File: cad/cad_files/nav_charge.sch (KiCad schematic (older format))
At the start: 26 parts

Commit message: Bring out battery charge status
LED1 flashes an LED to indicate charging/not-charging/error conditions
Connect it to a hierarchical pin for monitoring by microcontroller
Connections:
- net LED_1a renamed charge_status
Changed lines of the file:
@@
-EESchema Schematic File Version 2  date Tue 02 Dec 2014 10:18:06 PM HST
+EESchema Schematic File Version 2  date Tue 02 Dec 2014 11:16:27 PM HST
 LIBS:local_parts
 LIBS:power
@@
 $Descr A4 11700 8267
 encoding utf-8
-Sheet 2 4
+Sheet 3 4
 Title "Battery Charger"
 Date "3 dec 2014"
@@
 Comment4 ""
 $EndDescr
-Wire Wire Line
-	4200 4200 4200 4100
+Text HLabel 7900 2200 2    60   Output ~ 0
+charge_status
+Wire Wire Line
+	7900 2200 5200 2200
+Wire Wire Line
+	5200 2200 5200 3600
+Connection ~ 5600 3600
+Wire Wire Line
+	5200 3600 5600 3600
+Connection ~ 3800 4100
+Connection ~ 1500 3100
+Wire Wire Line
+	1500 4100 1500 1500
+Wire Wire Line
+	1500 4100 4200 4100
+Wire Wire Line
+	2400 2000 900  2000
+Connection ~ 3800 4900
+Wire Wire Line
+	5200 4900 3800 4900
+Connection ~ 4200 5900
+Wire Wire Line
+	4200 5900 3800 5900
+Wire Wire Line
+	3800 5900 3800 5800
+Wire Wire Line
+	3800 4100 3800 4200
+Wire Wire Line
+	3800 4700 3800 5300
+Wire Wire Line
+	1100 2400 1100 2200
+Wire Wire Line
+	1100 2200 900  2200
+Wire Wire Line
+	1500 3100 1900 3100
+Connection ~ 4000 2000
+Wire Wire Line
+	3900 2000 7700 2000
+Connection ~ 7700 5200
+Wire Wire Line
+	7700 5200 7900 5200
+Wire Wire Line
+	5200 4500 4500 4500
+Connection ~ 6700 6500
+Wire Wire Line
+	6700 6500 6700 5100
+Connection ~ 6000 6500
+Wire Wire Line
+	7700 6500 5800 6500
+Wire Wire Line
+	5800 6500 5800 6400
+Wire Wire Line
+	5800 5700 5800 5900
+Wire Wire Line
+	7600 5300 7700 5300
+Wire Wire Line
+	7100 5300 6800 5300
+Wire Wire Line
+	6800 5300 6800 4900
+Wire Wire Line
+	6800 4900 6600 4900
+Wire Wire Line
+	7700 4200 7700 4500
+Connection ~ 7700 2700
+Wire Wire Line
+	7700 2000 7700 2900
+Wire Wire Line
+	5200 4700 5100 4700
+Wire Wire Line
+	5100 4700 5100 4800
+Wire Wire Line
+	6600 4500 6700 4500
+Wire Wire Line
+	6700 4500 6700 3400
+Connection ~ 7700 3400
+Wire Wire Line
+	6700 3400 7700 3400
+Wire Wire Line
+	5600 2900 5600 3100
+Wire Wire Line
+	5900 3500 5900 3900
+Wire Wire Line
+	5900 2400 5900 1500
+Wire Wire Line
+	6200 3900 6200 3100
+Wire Wire Line
+	6200 3100 6400 3100
+Connection ~ 7000 3100
+Wire Wire Line
+	7000 3100 7000 2700
+Wire Wire Line
+	7000 2700 7100 2700
+Connection ~ 2600 3100
+Wire Wire Line
+	2600 2300 2600 3100
+Wire Wire Line
+	3000 2600 3000 2800
+Wire Wire Line
+	1700 2600 1700 2800
+Wire Wire Line
+	2800 1800 4000 1800
+Wire Wire Line
+	3300 2000 2800 2000
+Connection ~ 2100 2000
+Wire Wire Line
+	1700 2000 1700 2200
+Wire Wire Line
+	2100 2000 2100 2200
+Wire Wire Line
+	2400 1800 2200 1800
+Wire Wire Line
+	2200 1800 2200 2000
+Connection ~ 2200 2000
+Wire Wire Line
+	3000 2200 3000 2000
+Connection ~ 3000 2000
+Wire Wire Line
+	2100 2600 2100 2800
+Wire Wire Line
+	2400 3100 2800 3100
+Connection ~ 1700 2000
+Wire Wire Line
+	3300 3100 4500 3100
+Wire Wire Line
+	6900 3100 7400 3100
+Wire Wire Line
+	7600 2700 7700 2700
+Wire Wire Line
+	5900 2900 5900 3100
+Wire Wire Line
+	5700 3900 5700 3800
+Wire Wire Line
+	5700 3800 5600 3800
+Wire Wire Line
+	5600 3800 5600 3500
+Wire Wire Line
+	5600 2400 5600 2300
+Wire Wire Line
+	5600 2300 5900 2300
+Connection ~ 5900 2300
+Wire Wire Line
+	7700 3600 7700 3300
+Wire Wire Line
+	7700 4300 6900 4300
+Connection ~ 7700 4300
+Wire Wire Line
+	6900 4300 6900 4700
+Wire Wire Line
+	6900 4700 6600 4700
+Wire Wire Line
+	6700 5100 6600 5100
+Wire Wire Line
+	7700 5900 7700 5100
+Connection ~ 7700 5300
+Wire Wire Line
+	6000 5700 6000 5900
+Wire Wire Line
+	6000 6400 6000 6500
+Wire Wire Line
+	6100 6500 6100 5700
+Connection ~ 6100 6500
+Wire Wire Line
+	7700 3500 7900 3500
+Connection ~ 7700 3500
+Wire Wire Line
+	4500 3100 4500 4500
+Wire Wire Line
+	4000 1800 4000 2000
+Connection ~ 1500 2000
+Wire Wire Line
+	4200 4700 4200 5300
+Wire Wire Line
+	4200 5800 4200 6000
+Wire Wire Line
+	7700 6600 7700 6400
+Connection ~ 7700 6500
+Wire Wire Line
+	5200 5100 4200 5100
+Connection ~ 4200 5100
 Wire Wire Line
 	5900 1500 1500 1500
-Connection ~ 4200 5100
-Wire Wire Line
-	5200 5100 4200 5100
-Connection ~ 7700 6500
-Wire Wire Line
-	7700 6400 7700 6600
-Wire Wire Line
-	4200 6000 4200 5800
-Wire Wire Line
-	4200 5300 4200 4700
-Connection ~ 1500 2000
-Wire Wire Line
-	4000 2000 4000 1800
-Wire Wire Line
-	4500 3100 4500 4500
-Connection ~ 7700 3500
-Wire Wire Line
-	7700 3500 7900 3500
-Connection ~ 6100 6500
-Wire Wire Line
-	6100 6500 6100 5700
-Wire Wire Line
-	6000 6400 6000 6500
-Wire Wire Line
-	6000 5700 6000 5900
-Connection ~ 7700 5300
-Wire Wire Line
-	7700 5100 7700 5900
-Wire Wire Line
-	6600 5100 6700 5100
-Wire Wire Line
-	6600 4700 6900 4700
-Wire Wire Line
-	6900 4700 6900 4300
-Connection ~ 7700 4300
-Wire Wire Line
-	6900 4300 7700 4300
-Wire Wire Line
-	7700 3300 7700 3600
-Connection ~ 5900 2300
-Wire Wire Line
-	5900 2300 5600 2300
-Wire Wire Line
-	5600 2300 5600 2400
-Wire Wire Line
-	5600 3500 5600 3600
-Wire Wire Line
-	5600 3600 5700 3600
-Wire Wire Line
-	5700 3600 5700 3900
-Wire Wire Line
-	5900 2900 5900 3100
-Wire Wire Line
-	7600 2700 7700 2700
-Wire Wire Line
-	7400 3100 6900 3100
-Wire Wire Line
-	4500 3100 3300 3100
-Connection ~ 1700 2000
-Wire Wire Line
-	2800 3100 2400 3100
-Wire Wire Line
-	2100 2600 2100 2800
-Connection ~ 3000 2000
-Wire Wire Line
-	3000 2200 3000 2000
-Connection ~ 2200 2000
-Wire Wire Line
-	2200 2000 2200 1800
-Wire Wire Line
-	2200 1800 2400 1800
-Wire Wire Line
-	2100 2000 2100 2200
-Wire Wire Line
-	1700 2000 1700 2200
-Connection ~ 2100 2000
-Wire Wire Line
-	2800 2000 3300 2000
-Wire Wire Line
-	4000 1800 2800 1800
-Wire Wire Line
-	1700 2600 1700 2800
-Wire Wire Line
-	3000 2600 3000 2800
-Wire Wire Line
-	2600 2300 2600 3100
-Connection ~ 2600 3100
-Wire Wire Line
-	7100 2700 7000 2700
-Wire Wire Line
-	7000 2700 7000 3100
-Connection ~ 7000 3100
-Wire Wire Line
-	6400 3100 6200 3100
-Wire Wire Line
-	6200 3100 6200 3900
-Wire Wire Line
-	5900 1500 5900 2400
-Wire Wire Line
-	5900 3500 5900 3900
-Wire Wire Line
-	5600 2900 5600 3100
-Wire Wire Line
-	7700 3400 6700 3400
-Connection ~ 7700 3400
-Wire Wire Line
-	6700 3400 6700 4500
-Wire Wire Line
-	6700 4500 6600 4500
-Wire Wire Line
-	5100 4800 5100 4700
-Wire Wire Line
-	5100 4700 5200 4700
-Wire Wire Line
-	7700 2900 7700 2000
-Connection ~ 7700 2700
-Wire Wire Line
-	7700 4500 7700 4200
-Wire Wire Line
-	6600 4900 6800 4900
-Wire Wire Line
-	6800 4900 6800 5300
-Wire Wire Line
-	6800 5300 7100 5300
-Wire Wire Line
-	7600 5300 7700 5300
-Wire Wire Line
-	5800 5700 5800 5900
-Wire Wire Line
-	5800 6400 5800 6500
-Wire Wire Line
-	5800 6500 7700 6500
-Connection ~ 6000 6500
-Wire Wire Line
-	6700 5100 6700 6500
-Connection ~ 6700 6500
-Wire Wire Line
-	4500 4500 5200 4500
-Wire Wire Line
-	7700 5200 7900 5200
-Connection ~ 7700 5200
-Wire Wire Line
-	7700 2000 3900 2000
-Connection ~ 4000 2000
-Wire Wire Line
-	1500 3100 1900 3100
-Wire Wire Line
-	900  2200 1100 2200
-Wire Wire Line
-	1100 2200 1100 2400
-Wire Wire Line
-	3800 5300 3800 4700
-Wire Wire Line
-	3800 4100 3800 4200
-Wire Wire Line
-	3800 5800 3800 5900
-Wire Wire Line
-	3800 5900 4200 5900
-Connection ~ 4200 5900
-Wire Wire Line
-	5200 4900 3800 4900
-Connection ~ 3800 4900
-Wire Wire Line
-	900  2000 2400 2000
-Wire Wire Line
-	4200 4100 1500 4100
-Wire Wire Line
-	1500 4100 1500 1500
-Connection ~ 1500 3100
-Connection ~ 3800 4100
+Wire Wire Line
+	4200 4100 4200 4200
 Text Notes 8000 3700 0    60   ~ 0
 TODO: power path for charger voltage rail \n  (rather than cutting load power \n    while charging)
@@
 Text Label 5600 3000 2    60   ~ 0
 LED_1b
-Text Label 5700 3800 1    60   ~ 0
+Text Label 5600 3800 2    60   ~ 0
 LED_1a
 Text Label 6700 4900 0    60   ~ 0
@@
 	0    1    -1   0
 $EndComp
-Text Notes 5000 3800 0    60   ~ 0
+Text Notes 5400 4000 2    60   ~ 0
 LED2 prog:\nopen for 2S\nlow for 1S\nhigh for 2P
 Text Notes 8050 6050 0    60   ~ 0

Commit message: Adding refdes details for nav_charge
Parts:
- gave numbers to parts that had none: 17
- renumbered BT1 to BTp101, BT2 to BTp102, R10 to Rp109, R14 to Rp112
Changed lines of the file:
@@
-EESchema Schematic File Version 2  date Wed 03 Dec 2014 11:28:33 AM HST
+EESchema Schematic File Version 2  date Wed 03 Dec 2014 01:00:34 PM HST
 LIBS:local_parts
 LIBS:power
@@
 $EndComp
 $Comp
-L R Rp?
+L R Rp110
 U 1 1 53DA394C
 P 5800 6150
-F 0 "Rp?" V 5880 6150 50  0000 C CNN
+F 0 "Rp110" V 5880 6150 50  0000 C CNN
 F 1 "33k" V 5800 6150 50  0000 C CNN
 	1    5800 6150
@@
 $EndComp
 $Comp
-L R Rp?
+L R Rp111
 U 1 1 53DA3944
 P 6000 6150
-F 0 "Rp?" V 6080 6150 50  0000 C CNN
+F 0 "Rp111" V 6080 6150 50  0000 C CNN
 F 1 "120k" V 6000 6150 50  0000 C CNN
 	1    6000 6150
@@
 $EndComp
 $Comp
-L R R10
+L R Rp109
 U 1 1 53DA275B
 P 7350 5300
-F 0 "R10" V 7430 5300 50  0000 C CNN
+F 0 "Rp109" V 7430 5300 50  0000 C CNN
 F 1 "10" V 7350 5300 50  0000 C CNN
 	1    7350 5300
@@
 $EndComp
 $Comp
-L R R14
+L R Rp112
 U 1 1 53DA26C1
 P 7700 6150
-F 0 "R14" V 7780 6150 50  0000 C CNN
+F 0 "Rp112" V 7780 6150 50  0000 C CNN
 F 1 ".27" V 7700 6150 50  0000 C CNN
 	1    7700 6150
@@
 $EndComp
 $Comp
-L BATTERY BT2
+L BATTERY BTp102
 U 1 1 53DA259B
 P 7700 4800
-F 0 "BT2" H 7700 5000 50  0000 C CNN
+F 0 "BTp102" H 7700 5000 50  0000 C CNN
 F 1 "BATTERY" H 7700 4610 50  0000 C CNN
 	1    7700 4800
@@
 $EndComp
 $Comp
-L BATTERY BT1
+L BATTERY BTp101
 U 1 1 53DA2480
 P 7700 3900
-F 0 "BT1" H 7700 4100 50  0000 C CNN
+F 0 "BTp101" H 7700 4100 50  0000 C CNN
 F 1 "BATTERY" H 7700 3710 50  0000 C CNN
 	1    7700 3900
@@
 $EndComp
 $Comp
-L C C?
+L C Cp103
 U 1 1 53DA230B
 P 5900 3300
-F 0 "C?" H 5950 3400 50  0000 L CNN
+F 0 "Cp103" H 5950 3400 50  0000 L CNN
 F 1 "1uF" H 5950 3200 50  0000 L CNN
 	1    5900 3300
@@
 $EndComp
 $Comp
-L R Rp?
+L R Rp104
 U 1 1 53DA22FE
 P 5900 2650
-F 0 "Rp?" V 5980 2650 50  0000 C CNN
+F 0 "Rp104" V 5980 2650 50  0000 C CNN
 F 1 "150" V 5900 2650 50  0000 C CNN
 	1    5900 2650
@@
 NoConn ~ 5800 3900
 $Comp
-L PNP Qp?
+L PNP Qp102
 U 1 1 53DA21A7
 P 7600 3100
-F 0 "Qp?" H 7600 2950 60  0000 R CNN
+F 0 "Qp102" H 7600 2950 60  0000 R CNN
 F 1 "FCX718" H 7600 3250 60  0000 R CNN
 	1    7600 3100
@@
 $EndComp
 $Comp
-L R Rp?
+L R Rp105
 U 1 1 53DA21A3
 P 7350 2700
-F 0 "Rp?" V 7430 2700 50  0000 C CNN
+F 0 "Rp105" V 7430 2700 50  0000 C CNN
 F 1 "10k" V 7350 2700 50  0000 C CNN
 	1    7350 2700
@@
 $EndComp
 $Comp
-L R Rp?
+L R Rp106
 U 1 1 53DA219B
 P 6650 3100
-F 0 "Rp?" V 6730 3100 50  0000 C CNN
+F 0 "Rp106" V 6730 3100 50  0000 C CNN
 F 1 "100" V 6650 3100 50  0000 C CNN
 	1    6650 3100
@@
 $EndComp
 $Comp
-L R Rp?
+L R Rp103
 U 1 1 53DA2133
 P 5600 2650
-F 0 "Rp?" V 5680 2650 50  0000 C CNN
+F 0 "Rp103" V 5680 2650 50  0000 C CNN
 F 1 "270" V 5600 2650 50  0000 C CNN
 	1    5600 2650
@@
 $EndComp
 $Comp
-L LED D?
+L LED Dp103
 U 1 1 53DA211C
 P 5600 3300
-F 0 "D?" H 5600 3400 50  0000 C CNN
+F 0 "Dp103" H 5600 3400 50  0000 C CNN
 F 1 "LED" H 5600 3200 50  0000 C CNN
 	1    5600 3300
@@
 $EndComp
 $Comp
-L DS2712 Up?
+L DS2712 Up101
 U 1 1 53DA0E27
 P 5900 4800
-F 0 "Up?" H 5900 4700 50  0000 C CNN
+F 0 "Up101" H 5900 4700 50  0000 C CNN
 F 1 "DS2712" H 5900 4900 50  0000 C CNN
 F 2 "MODULE" H 5900 4800 50  0001 C CNN
@@
 $EndComp
 $Comp
-L R Rp?
+L R Rp102
 U 1 1 53DA0CD8
 P 3050 3100
-F 0 "Rp?" V 3130 3100 50  0000 C CNN
+F 0 "Rp102" V 3130 3100 50  0000 C CNN
 F 1 "0" V 3050 3100 50  0000 C CNN
 	1    3050 3100
@@
 $EndComp
 $Comp
-L R Rp?
+L R Rp101
 U 1 1 53DA0CB2
 P 2150 3100
-F 0 "Rp?" V 2230 3100 50  0000 C CNN
+F 0 "Rp101" V 2230 3100 50  0000 C CNN
 F 1 "330" V 2150 3100 50  0000 C CNN
 	1    2150 3100
@@
 $EndComp
 $Comp
-L DIODE D?
+L DIODE Dp102
 U 1 1 53D8CC6B
 P 3000 2400
-F 0 "D?" H 3000 2500 40  0000 C CNN
+F 0 "Dp102" H 3000 2500 40  0000 C CNN
 F 1 "DIODE" H 3000 2300 40  0000 C CNN
 	1    3000 2400
@@
 $EndComp
 $Comp
-L DIODE D?
+L DIODE Dp101
 U 1 1 53D8CC68
 P 2600 1800
-F 0 "D?" H 2600 1900 40  0000 C CNN
+F 0 "Dp101" H 2600 1900 40  0000 C CNN
 F 1 "DIODE" H 2600 1700 40  0000 C CNN
 	1    2600 1800
@@
 $EndComp
 $Comp
-L C C?
+L C Cp102
 U 1 1 53D8CC32
 P 2100 2400
-F 0 "C?" H 2150 2500 50  0000 L CNN
+F 0 "Cp102" H 2150 2500 50  0000 L CNN
 F 1 "0.1uF" H 2150 2300 50  0000 L CNN
 	1    2100 2400
@@
 $EndComp
 $Comp
-L C C?
+L C Cp101
 U 1 1 53D8CC30
 P 1700 2400
-F 0 "C?" H 1750 2500 50  0000 L CNN
+F 0 "Cp101" H 1750 2500 50  0000 L CNN
 F 1 "47uF" H 1750 2300 50  0000 L CNN
 	1    1700 2400
@@
 $EndComp
 $Comp
-L MOSFET_P Q?
+L MOSFET_P Qp101
 U 1 1 53D8CBBC
 P 2600 2100
-F 0 "Q?" H 2600 2290 60  0000 R CNN
+F 0 "Qp101" H 2600 2290 60  0000 R CNN
 F 1 "ZXM62P02E6" H 2600 1920 60  0000 R CNN
 	1    2600 2100

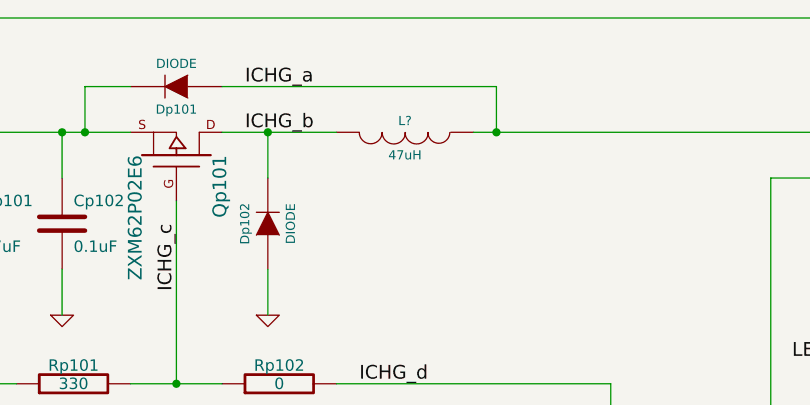
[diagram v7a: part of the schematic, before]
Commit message: Add refdes for inductor
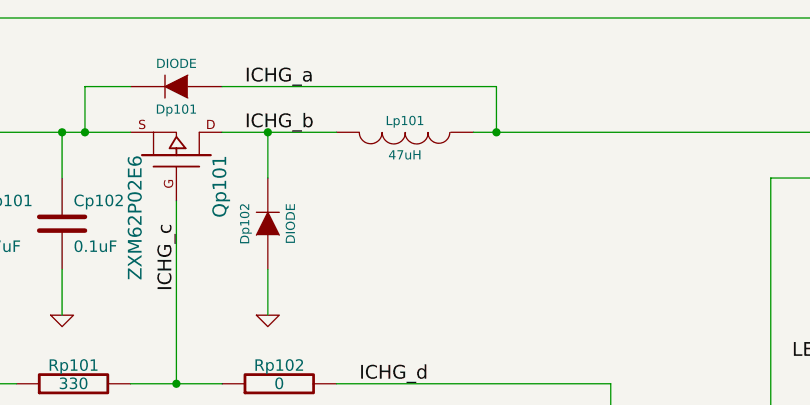
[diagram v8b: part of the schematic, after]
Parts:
- gave numbers to parts that had none: 1
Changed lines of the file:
@@
-EESchema Schematic File Version 2  date Wed 03 Dec 2014 05:36:01 PM HST
+EESchema Schematic File Version 2  date Wed 03 Dec 2014 05:36:52 PM HST
 LIBS:local_parts
 LIBS:power
@@
 thm1
 $Comp
-L GND #PWR?
+L GND #PWR08
 U 1 1 53DB3075
 P 7700 6600
-F 0 "#PWR?" H 7700 6600 30  0001 C CNN
+F 0 "#PWR08" H 7700 6600 30  0001 C CNN
 F 1 "GND" H 7700 6530 30  0001 C CNN
 	1    7700 6600
@@
 $EndComp
 $Comp
-L GND #PWR?
+L GND #PWR09
 U 1 1 53DB304B
 P 4200 6000
-F 0 "#PWR?" H 4200 6000 30  0001 C CNN
+F 0 "#PWR09" H 4200 6000 30  0001 C CNN
 F 1 "GND" H 4200 5930 30  0001 C CNN
 	1    4200 6000
@@
 WHY!?
 $Comp
-L GND #PWR?
+L GND #PWR010
 U 1 1 53DA2C30
 P 5100 4800
-F 0 "#PWR?" H 5100 4800 30  0001 C CNN
+F 0 "#PWR010" H 5100 4800 30  0001 C CNN
 F 1 "GND" H 5100 4730 30  0001 C CNN
 	1    5100 4800
@@
 $EndComp
 $Comp
-L GND #PWR?
+L GND #PWR011
 U 1 1 53DA0DD7
 P 1100 2400
-F 0 "#PWR?" H 1100 2400 30  0001 C CNN
+F 0 "#PWR011" H 1100 2400 30  0001 C CNN
 F 1 "GND" H 1100 2330 30  0001 C CNN
 	1    1100 2400
@@
 $EndComp
 $Comp
-L GND #PWR?
+L GND #PWR012
 U 1 1 53DA0D36
 P 1700 2800
-F 0 "#PWR?" H 1700 2800 30  0001 C CNN
+F 0 "#PWR012" H 1700 2800 30  0001 C CNN
 F 1 "GND" H 1700 2730 30  0001 C CNN
 	1    1700 2800
@@
 $EndComp
 $Comp
-L GND #PWR?
+L GND #PWR013
 U 1 1 53DA0D33
 P 2100 2800
-F 0 "#PWR?" H 2100 2800 30  0001 C CNN
+F 0 "#PWR013" H 2100 2800 30  0001 C CNN
 F 1 "GND" H 2100 2730 30  0001 C CNN
 	1    2100 2800
@@
 $EndComp
 $Comp
-L GND #PWR?
+L GND #PWR014
 U 1 1 53DA0D2E
 P 3000 2800
-F 0 "#PWR?" H 3000 2800 30  0001 C CNN
+F 0 "#PWR014" H 3000 2800 30  0001 C CNN
 F 1 "GND" H 3000 2730 30  0001 C CNN
 	1    3000 2800
@@
 $EndComp
 $Comp
-L INDUCTOR L?
+L INDUCTOR Lp101
 U 1 1 53D8CC47
 P 3600 2000
-F 0 "L?" V 3550 2000 40  0000 C CNN
+F 0 "Lp101" V 3550 2000 40  0000 C CNN
 F 1 "47uH" V 3700 2000 40  0000 C CNN
 	1    3600 2000
